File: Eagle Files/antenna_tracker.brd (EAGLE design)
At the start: 71.9 x 99.9 mm, 90 parts, among them IC1 ATMEGA1280-16AU, IC2 L298, Q11 BSS138, Q12 BSS138, Q8 16MHz, U1 LSM303DLHC, U2 MIC5219-3.3V, U4 FT232RL-BASICSSOP, U5 LD1117, X2 KUSBVX-BS1N

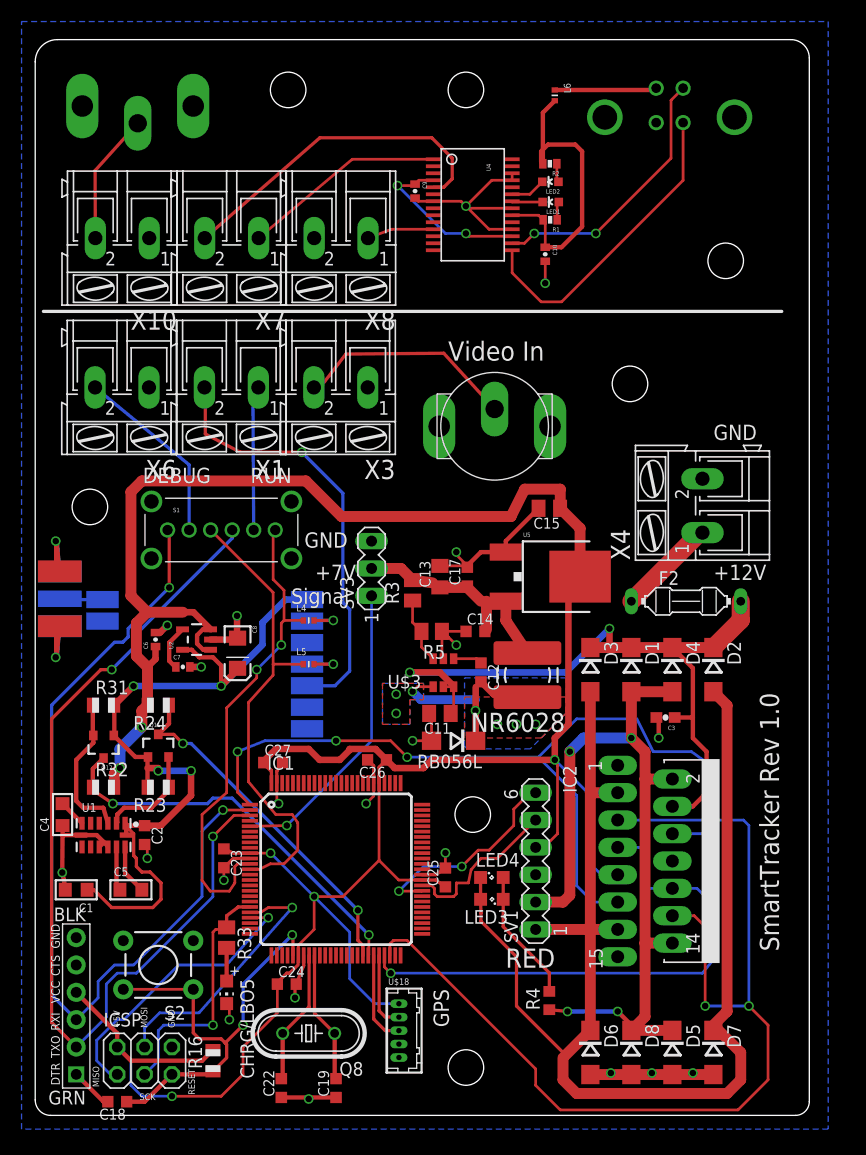
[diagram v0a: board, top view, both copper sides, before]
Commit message: Switched to 9DOF IC and a new 7.2V Buck Convertor
Added LSM9DS0 and MC34063
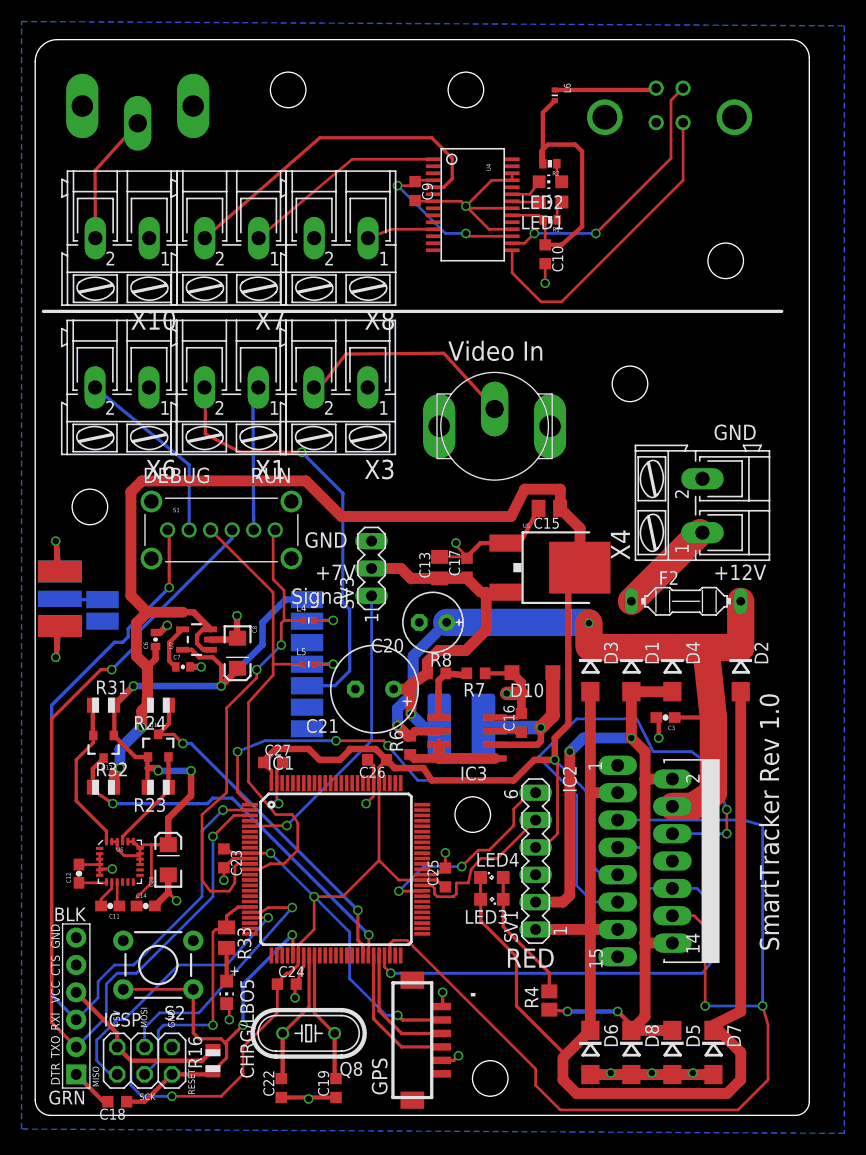
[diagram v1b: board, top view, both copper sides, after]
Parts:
- removed C1: 10µF, microbuilder:_0805
- removed C2: 0.1uF, rcl:C0603K
- removed C4: 4.70µF, microbuilder:_0805
- removed C5: 0.22µF, microbuilder:_0805
- removed NR6028: 4.7uH, resistor:POWER-CHOKE_WE-TPC
- removed R3: 50k, rcl:M0805
- removed R5: 6.34k, rcl:M0805
- removed RB056L: (no value), diode:DO214AC
- removed U$18: DF13-5P-1.25DSA, pixhawk2:DF13-5P-1.25DSA
- removed U$3: AP3211, antenna_tracker:AP3211
- removed U1: LSM303DLHC, microbuilder:LGA14
- added C16: 270pF, resistor:C0603K
- added C20: 100uF, rcl:E2,5-6E
- added C21: 470uF, rcl:E3,5-8
- added C28: 10uF, SparkFun-Capacitors:EIA3216
- added D10: 1N5819, diode:SOD123
- added IC3: MC34063AD, mc34063:SOIC8
- added J203: DF13C-6P-1.25V, con-hirose-df13:DF13C-6P-1.25V
- added L2: 15uH, rcl:POWER-CHOKE_WE-TPC
- added R6: 0.20R, rcl:R0603
- added R7: 820R, resistor:R0603
- added R8: 3.9K, rcl:R0603
- added U6: LSM9DS0, SparkFun-DigitalIC:LGA-24
- C10, C9: device SparkFun:0402-CAP -> resistor:C0603K
- C11: value 10uF -> 0.22uF; device rcl:C0805K -> SparkFun-Capacitors:0603-CAP
- C12: value 10nF -> 4.7uF; device rcl:C0603K -> SparkFun-Capacitors:0603-CAP
- C14: value 22uF -> 1.0uF; device rcl:C0603K -> SparkFun-Capacitors:0603-CAP
- LED1, LED2: device SparkFun:LED-0603 -> led:CHIP-LED0805
- LED3, LED4: value (none) -> Orange
- R4: value (none) -> 1k; device resistor:R0603 -> resistor:R0805
- moved C12 41.8 mm to (4.07, 22.4), turned to 90 degrees
- moved C14 39.9 mm to (10.3, 19.4)
- moved C11 35.5 mm to (6.96, 19.4)
- moved D2 2.54 mm to (65.5, 41.4)
- moved STANDOFF7 2.48 mm to (42.3, 3.43)
- moved C13 0.84 mm to (37.6, 50.9)
- moved C17 0.84 mm to (40.1, 50.9)
- moved U5 0.84 mm to (49.0, 50.9)
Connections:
- removed net DRDY: U1.9
- removed net INT1: U1.5
- removed net INT2: U1.4
- removed net N$1: C5.2, U1.13
- removed net N$3: C4.2, U1.6
- removed net N$4: C5.1, U1.12
- new net DEN_G: U6.10
- new net DRDY_G: U6.12
- new net INT1_XM: U6.13
- new net INT2_XM: U6.14
- new net INT_G: U6.11
- new net N$19: C16.1, IC3.3
- new net N$30: IC3.1, IC3.7, IC3.8, R6.1
- new net N$31: IC3.5, R7.2, R8.2
- new net N$32: D10.C, IC3.2, L2.1
- net +12V: now also C20.+, IC3.6, R6.2; no longer C11.1, U$3.P$4, U$3.P$5
- net +3V3: now also C14.1, C28.A, U6.15, U6.16, U6.17, U6.18, U6.19, U6.20, U6.22, U6.23; no longer C1.1, C2.1, U1.1, U1.14
- net +5V: now also J203.2; no longer U$18.1
- net +7V: now also C21.+, L2.2, R8.1; no longer C14.2, NR6028.2, R3.2
- net GND: now also C12.2, C14.2, C16.2, C20.-, C21.-, C28.C, D10.A, IC3.4, J203.1, J203.5, R7.1, U6.2, U6.3, U6.4, U6.5, U6.6; no longer C1.2, C11.2, C14.1, C2.2, C4.1, R5.1, RB056L.A, U$18.5, U$3.P$2, U1.10, U1.11, U1.7
- net N$28: now also C11.2, U6.8; no longer C12.2, NR6028.1, RB056L.C, U$3.P$6
- net N$29: now also C12.1, U6.7; no longer R3.1, R5.2, U$3.P$3
- net N$7: now also C11.1, U6.9; no longer C12.1, U$3.P$1
- net RX1: now also J203.4; no longer U$18.3
- net SCL: now also U6.21; no longer U1.2
- net SDA: now also U6.24; no longer U1.3
- net TX1: now also J203.3; no longer U$18.2
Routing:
- net N$32: track 0.00 -> 16.6 mm, vias 0 -> 1
- net N$28: track 18.8 -> 2.64 mm, vias 7 -> 0
- net +7V: track 22.1 -> 35.2 mm, vias 0 -> 1
- net N$30: track 0.00 -> 9.31 mm
- net +12V: track 67.3 -> 73.7 mm
- net N$31: track 0.00 -> 6.38 mm
- net +5V: track 271.0 -> 276.7 mm, vias 6 -> 7
- net N$1: track 4.62 -> 0.00 mm
- net TX1: track 7.23 -> 11.8 mm
- net RX1: track 8.70 -> 13.3 mm
- net +3V3: track 72.5 -> 68.0 mm
- net N$4: track 4.11 -> 0.00 mm
- net ENABLE: track 81.7 -> 85.4 mm
- net N$29: track 6.19 -> 2.58 mm
- net N$3: track 2.57 -> 0.00 mm
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- removed copper zone on layer 1, net N$28
- removed copper zone on layer 16, net N$28
